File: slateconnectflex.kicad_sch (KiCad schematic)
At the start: 2 parts, among them CN4 DF40C-40DS-0.4V, CN6 DF40C-40DS-0.4V

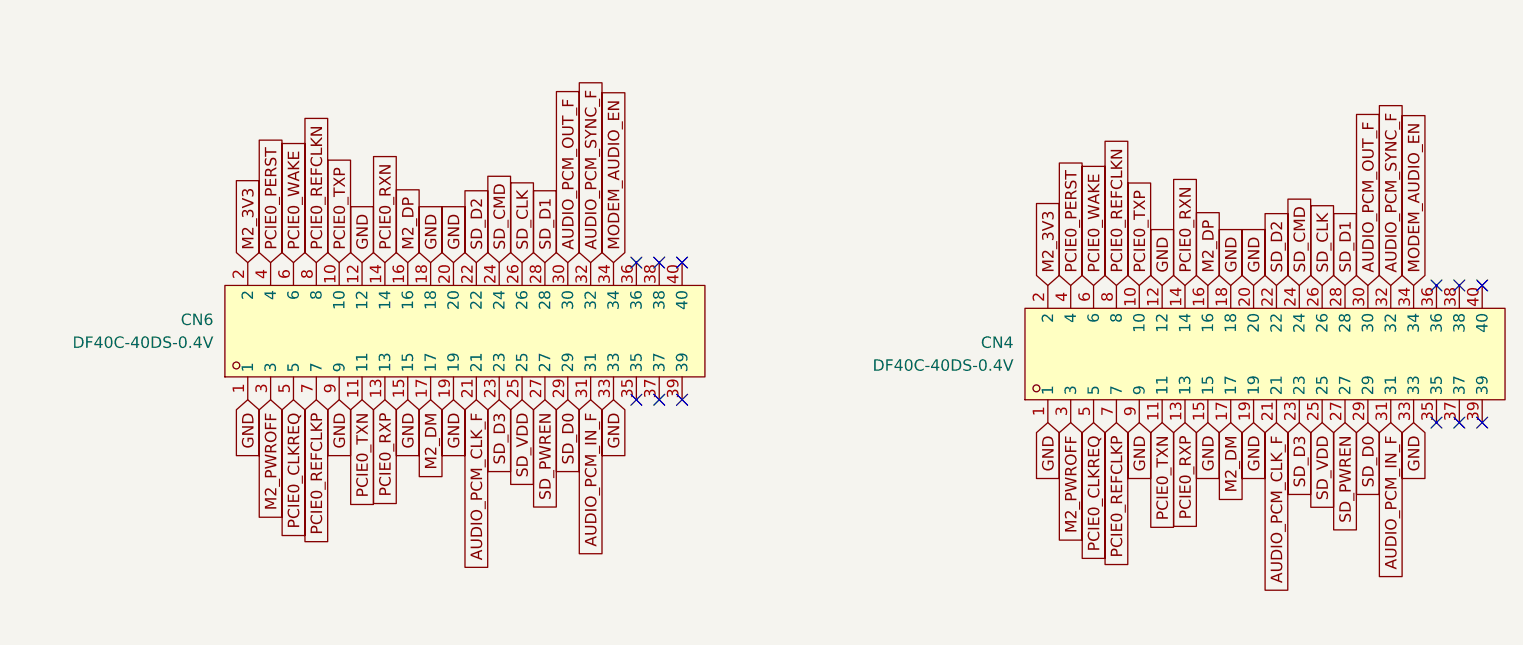
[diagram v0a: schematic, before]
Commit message: finished slateconnect i2c gpio expander, completed led status bar schematic, fixed all drc errors, started assigning footprints and started bom
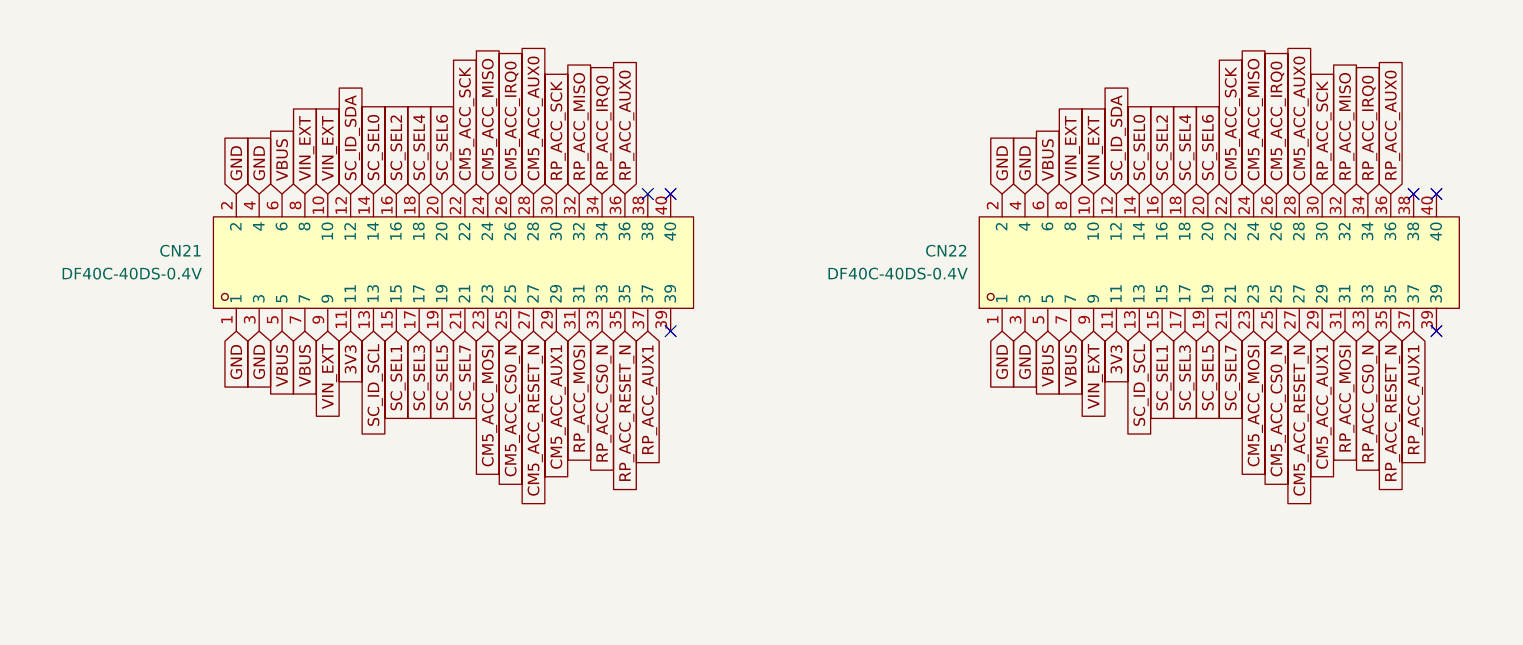
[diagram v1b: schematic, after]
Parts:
- removed CN4, CN6: DF40C-40DS-0.4V, slate113:CONN-SMD_DF40C-40DS-0.4V51, symbol slate113:DF40C-40DS-0.4V
- added CN21, CN22: DF40C-40DS-0.4V, slate113:CONN-SMD_DF40C-40DS-0.4V51, symbol slate113:DF40C-40DS-0.4V
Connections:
- net GND: now also CN21.1, CN21.2, CN21.3, CN21.4, CN22.1, CN22.2, CN22.3, CN22.4
- new net 3V3: CN21.11, CN22.11
- new net CM5_ACC_AUX0: CN21.28, CN22.28
- new net CM5_ACC_AUX1: CN21.29, CN22.29
- new net CM5_ACC_CS0_N: CN21.25, CN22.25
- new net CM5_ACC_IRQ0: CN21.26, CN22.26
- new net CM5_ACC_MISO: CN21.24, CN22.24
- new net CM5_ACC_MOSI: CN21.23, CN22.23
- new net CM5_ACC_RESET_N: CN21.27, CN22.27
- new net CM5_ACC_SCK: CN21.22, CN22.22
- new net RP_ACC_AUX0: CN21.36, CN22.36
- new net RP_ACC_AUX1: CN21.37, CN22.37
- new net RP_ACC_CS0_N: CN21.33, CN22.33
- new net RP_ACC_IRQ0: CN21.34, CN22.34
- new net RP_ACC_MISO: CN21.32, CN22.32
- new net RP_ACC_MOSI: CN21.31, CN22.31
- new net RP_ACC_RESET_N: CN21.35, CN22.35
- new net RP_ACC_SCK: CN21.30, CN22.30
- new net SC_ID_SCL: CN21.13, CN22.13
- new net SC_ID_SDA: CN21.12, CN22.12
- new net SC_SEL0: CN21.14, CN22.14
- new net SC_SEL1: CN21.15, CN22.15
- new net SC_SEL2: CN21.16, CN22.16
- new net SC_SEL3: CN21.17, CN22.17
- new net SC_SEL4: CN21.18, CN22.18
- new net SC_SEL5: CN21.19, CN22.19
- new net SC_SEL6: CN21.20, CN22.20
- new net SC_SEL7: CN21.21, CN22.21
- new net VBUS: CN21.5, CN21.6, CN21.7, CN22.5, CN22.6, CN22.7
- new net VIN_EXT: CN21.10, CN21.8, CN21.9, CN22.10, CN22.8, CN22.9
- no-connect marks 12 -> 6

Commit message: finished m.2 board and copper pours, completed antenna bracket and power board, finished slateconnect board, reorganized libraries
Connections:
- net SC_SEL0: no longer names the net of CN22.14
- net SC_SEL0: no longer CN21.14
- net SC_SEL1: no longer names the net of CN22.15
- net SC_SEL1: no longer CN21.15
- net SC_SEL2: no longer names the net of CN22.16
- net SC_SEL2: no longer CN21.16
- net SC_SEL3: no longer names the net of CN22.17
- net SC_SEL3: no longer CN21.17
- net SC_SEL4: no longer names the net of CN22.18
- net SC_SEL4: no longer CN21.18
- net SC_SEL5: no longer names the net of CN22.19
- net SC_SEL5: no longer CN21.19
- net SC_SEL6: no longer names the net of CN22.20
- net SC_SEL6: no longer CN21.20
- net SC_SEL7: no longer names the net of CN22.21
- net SC_SEL7: no longer CN21.21
- no-connect marks 6 -> 22
